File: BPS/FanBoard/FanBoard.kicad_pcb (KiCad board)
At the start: 2 copper layers, 31.8 x 38.1 mm, 18 parts, among them J1 Conn_01x02, J2 Conn_01x02, J3 Conn_01x02, J4 Conn_01x02, Q1 BUK9M34-100EX, Q2 BUK9M34-100EX, Q3 BUK9M34-100EX, Q4 BUK9M34-100EX

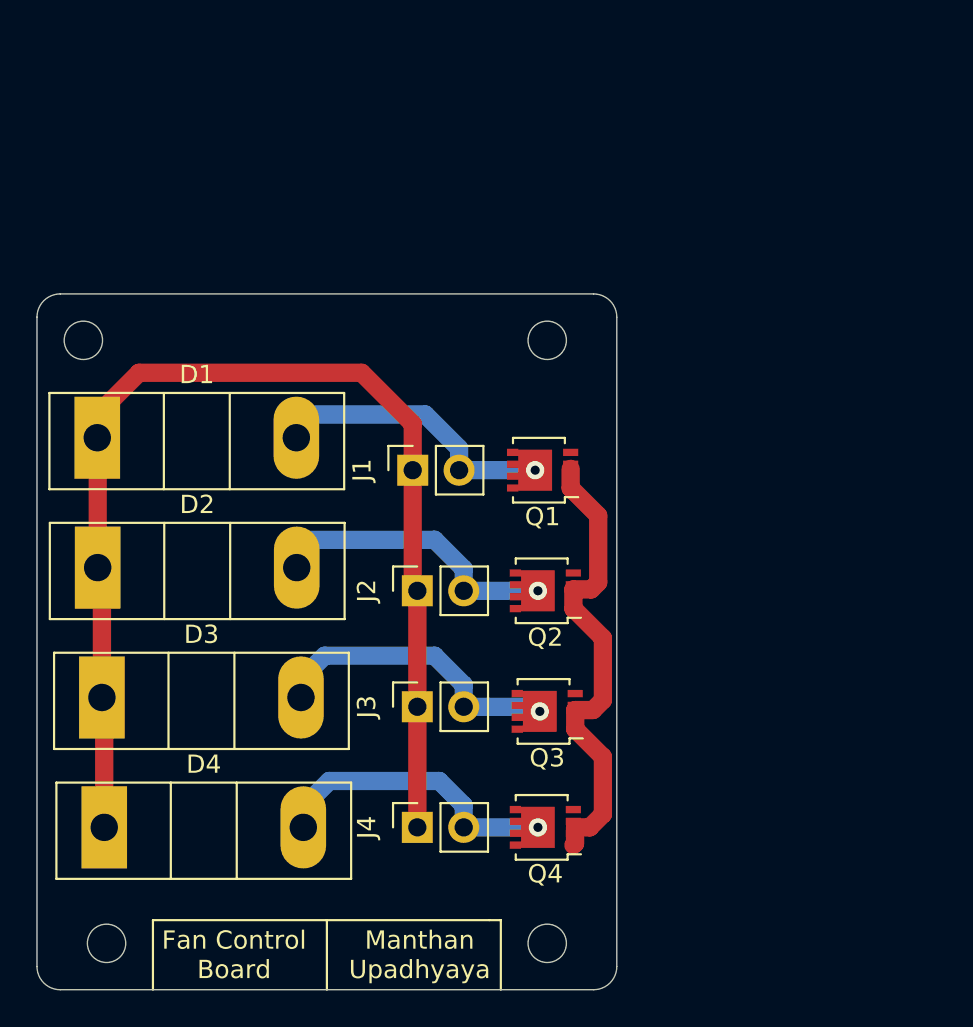
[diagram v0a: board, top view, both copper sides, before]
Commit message: Finished Fan Board PCB
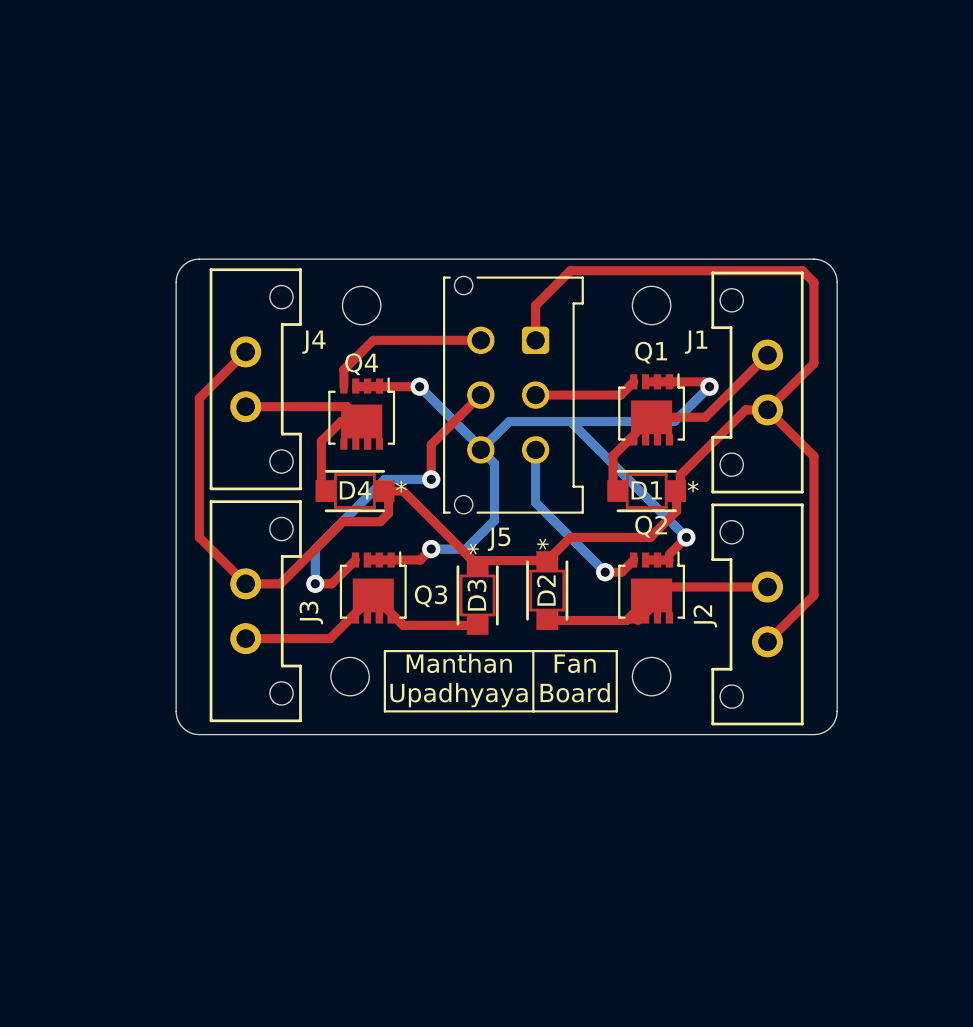
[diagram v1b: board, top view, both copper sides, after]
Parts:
- removed the G*** at (146.7, 89.5)
- removed the REF** at (134.6, 69.8)
- removed the REF** at (135.9, 102.9)
- removed the REF** at (160.0, 102.9)
- removed the REF** at (160.0, 69.8)
- added G***: LOGO, UTSVT_Special:Hallock_Image_Small, B.Cu at (165.4, 77.7)
- added J5: LDRBRDConn, Connector_Molex:Molex_Micro-Fit_3.0_43045-0612_2x03_P3.00mm_Vertical, F.Cu at (159.4, 69.8)
- added REF**: MountingHole_2.1mm, MountingHole:MountingHole_2.1mm, F.Cu at (165.7, 67.9)
- added REF**: MountingHole_2.1mm, MountingHole:MountingHole_2.1mm, F.Cu at (149.9, 67.9)
- added REF**: MountingHole_2.1mm, MountingHole:MountingHole_2.1mm, F.Cu at (165.7, 88.3)
- added REF**: MountingHole_2.1mm, MountingHole:MountingHole_2.1mm, F.Cu at (149.2, 88.3)
- D1, D2, D3, D4: value C3D25170H -> V22F22HM3; footprint Package_TO_SOT_THT:TO-247-2_Vertical -> UTSVT_BPS:V2F22HM
- J1, J2, J3, J4: footprint Connector_PinSocket_2.54mm:PinSocket_1x02_P2.54mm_Vertical -> UTSVT_Connectors:Molex_MicroFit3.0_1x2xP3.00mm_PolarizingPeg_Vertical
- moved D1 30.2 mm to (165.5, 78.1), turned to 180 degrees
- moved J4 27.7 mm to (143.5, 70.5), turned to 270 degrees
- moved Q4 24.8 mm to (149.9, 73.9), turned to 270 degrees
- moved D2 24.6 mm to (160.0, 83.6), turned to 270 degrees
- moved D4 23.0 mm to (149.5, 78.1), turned to 180 degrees
- moved D3 21.3 mm to (156.2, 83.8), turned to 270 degrees
- moved G*** 20.5 mm to (149.6, 75.2), turned to 180 degrees
- moved J1 19.7 mm to (172.1, 73.7)
- moved J2 19.4 mm to (172.1, 86.4)
- moved Q3 11.7 mm to (150.5, 83.4), turned to 270 degrees
- moved J3 11.6 mm to (143.5, 83.2), turned to 270 degrees
- moved Q1 6.82 mm to (165.7, 73.7), turned to 270 degrees
- moved Q2 5.82 mm to (165.7, 83.4), turned to 270 degrees
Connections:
- net GND renamed GNDPWR
- Q1 pad 4: Net-(Q1-Pad4) -> /FAN1
- Q2 pad 4: Net-(Q2-Pad4) -> /FAN2
- Q3 pad 4: Net-(Q3-Pad4) -> /FAN3
- Q4 pad 4: Net-(Q4-Pad4) -> /FAN4
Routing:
- net +12V: track 64.3 -> 93.6 mm
- net GNDPWR: track 26.0 -> 49.4 mm, vias 0 -> 4
- net /FAN3: track 0.00 -> 18.3 mm, vias 0 -> 2
- net /FAN2: track 0.00 -> 10.2 mm, vias 0 -> 1
- net /FAN4: track 0.00 -> 9.06 mm
- net /FAN1: track 0.00 -> 5.68 mm
- net Net-(D4-Pad2): track 16.3 -> 12.1 mm, vias 1 -> 0
- net Net-(D1-Pad2): track 15.9 -> 12.7 mm, vias 1 -> 0
- net Net-(D2-Pad2): track 16.3 -> 13.9 mm, vias 1 -> 0
- net Net-(D3-Pad2): track 16.6 -> 14.4 mm, vias 1 -> 0
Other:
- board size 31.8 x 38.1 mm -> 36.2 x 26 mm
- board text added: "Fan Board"
- board text removed: "Fan Control Board"

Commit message: Redid layout of board
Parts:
- removed G***: LOGO, UTSVT_Special:Hallock_Image_Small
- removed G***: LOGO, UTSVT_Special:UTSVT_Logo_Symbol
- removed J1: Conn_01x02, UTSVT_Connectors:Molex_MicroFit3.0_1x2xP3.00mm_PolarizingPeg_Vertical
- removed J5: LDRBRDConn, Connector_Molex:Molex_Micro-Fit_3.0_43045-0612_2x03_P3.00mm_Vertical
- removed REF** (x4): MountingHole_2.1mm, MountingHole:MountingHole_2.1mm
- added FAN1: Conn_01x02, UTSVT_Connectors:Molex_MicroFit3.0_1x2xP3.00mm_PolarizingPeg_Vertical, F.Cu at (176.3, 80.8)
- added H1: MountingHole, MountingHole:MountingHole_3mm, F.Cu at (146.1, 59.7)
- added H2: MountingHole, MountingHole:MountingHole_3mm, F.Cu at (146.1, 85.1)
- added H3: MountingHole, MountingHole:MountingHole_3mm, F.Cu at (168.9, 59.7)
- added H4: MountingHole, MountingHole:MountingHole_3mm, F.Cu at (168.9, 85.1)
- added LDRBRDConn: LDRBRDConn, Connector_Molex:Molex_Micro-Fit_3.0_43045-0612_2x03_P3.00mm_Vertical, F.Cu at (161.0, 66.4)
- moved FAN3 36.4 mm to (176.2, 67.3), turned to 90 degrees
- moved FAN2 33.9 mm to (139.1, 78.2), turned to 270 degrees
- moved Q3 25.2 mm to (168.1, 65.5), turned to 0 degrees
- moved D3 24.1 mm to (172.0, 65.7), turned to 90 degrees
- moved Q2 18.9 mm to (147.3, 79.6), turned to 180 degrees
- moved D2 17.0 mm to (143.4, 79.6)
- moved D4 13.6 mm to (143.7, 65.8), turned to 270 degrees
- moved Q4 8.02 mm to (148.0, 66.1), turned to 180 degrees
- moved FAN4 7.61 mm to (139.1, 64.3)
- moved D1 6.55 mm to (171.9, 79.4), turned to 90 degrees
- moved Q1 5.60 mm to (167.6, 78.9), turned to 0 degrees
- renumbered J2 to FAN2, J3 to FAN3, J4 to FAN4
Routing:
- net +12V: track 93.6 -> 0.00 mm, vias 0 -> 4
- net GNDPWR: track 49.4 -> 0.00 mm, vias 4 -> 0
- net /FAN1: track 5.68 -> 19.6 mm, vias 0 -> 1
- net Net-(D3-Pad2): track 14.4 -> 8.37 mm
- net Net-(D2-Pad2): track 13.9 -> 8.39 mm
- net /FAN2: track 10.2 -> 15.0 mm
- net Net-(D1-Pad2): track 12.7 -> 8.84 mm
- net Net-(D4-Pad2): track 12.1 -> 9.08 mm
- net /FAN4: track 9.06 -> 7.58 mm, vias 0 -> 1
- net /FAN3: track 18.3 -> 17.8 mm, vias 2 -> 1
- added copper zone on B.Cu, net +12V
- added copper zone on F.Cu, net GNDPWR
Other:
- board outline removed
- board text added: "12V"
- board text added: "FAN1"
- board text added: "FAN2"
- board text added: "FAN3"
- board text added: "FAN4"
- board text added: "GND"

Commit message: Finishing touches
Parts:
- added G***: LOGO, UTSVT_Special:Hallock_Image_Small, B.Cu at (152.4, 75.6)
- added G***: LOGO, UTSVT_Special:UTSVT_Logo_Symbol, B.Cu at (166.4, 76.2)
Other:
- board outline added: 45.1 x 33 mm

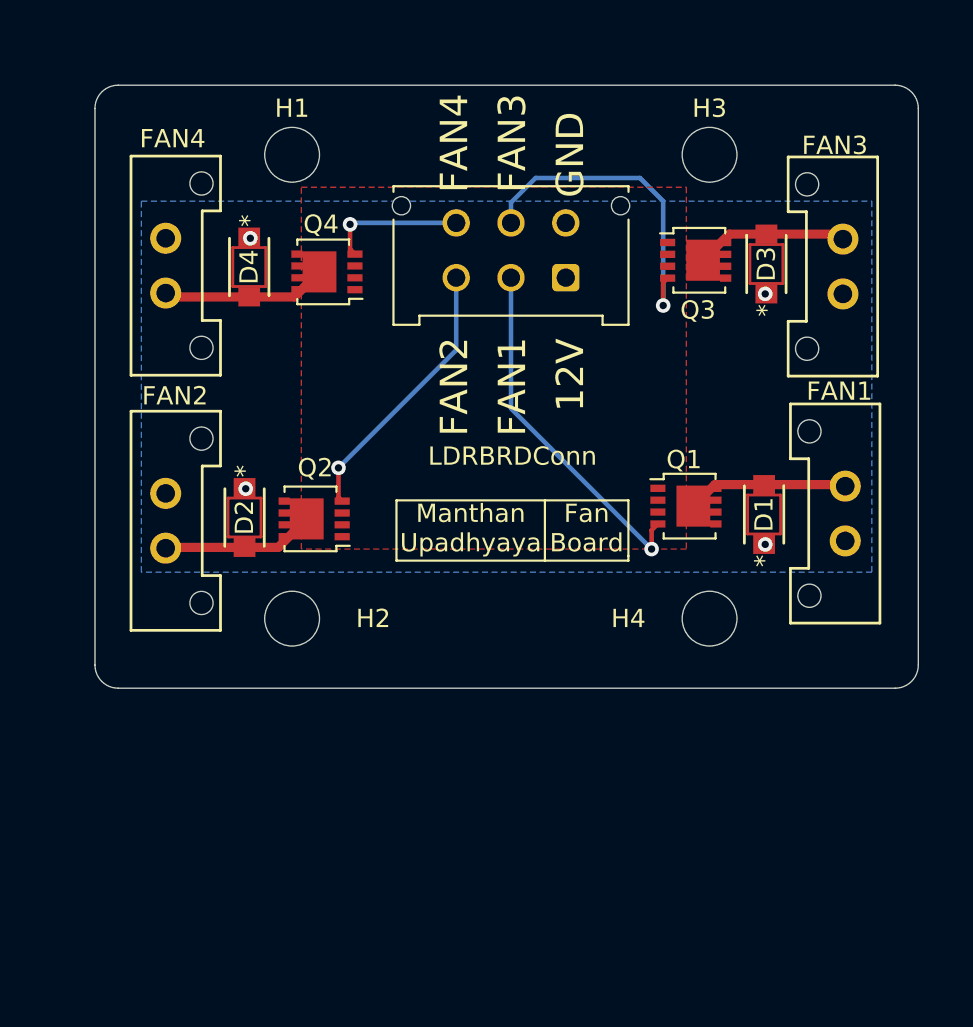
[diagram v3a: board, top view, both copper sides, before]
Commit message: Added status LED
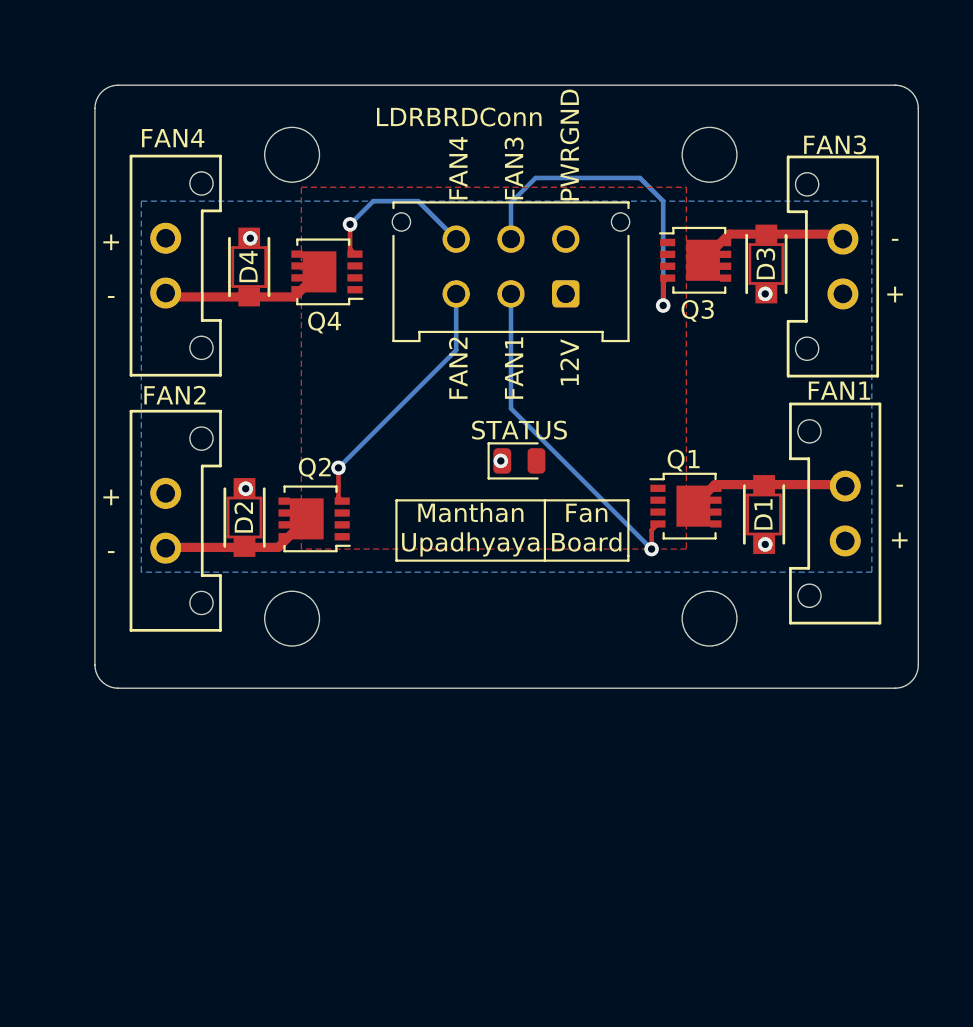
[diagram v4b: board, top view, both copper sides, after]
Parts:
- added STATUS: LED, LED_SMD:LED_0805_2012Metric, F.Cu at (158.5, 76.5)
- LDRBRDConn: value LDRBRDConn -> Conn_02x03
- moved LDRBRDConn 0.89 mm to (161.0, 67.3)
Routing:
- net /FAN4: track 7.58 -> 9.05 mm
- net /FAN3: track 17.8 -> 18.7 mm
- net /FAN2: track 15.0 -> 14.1 mm
- net /FAN1: track 19.6 -> 18.7 mm
- net +12V: vias 4 -> 5
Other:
- board text added: "+"
- board text added: "-"
- board text added: "PWRGND"
- board text removed: "GND"

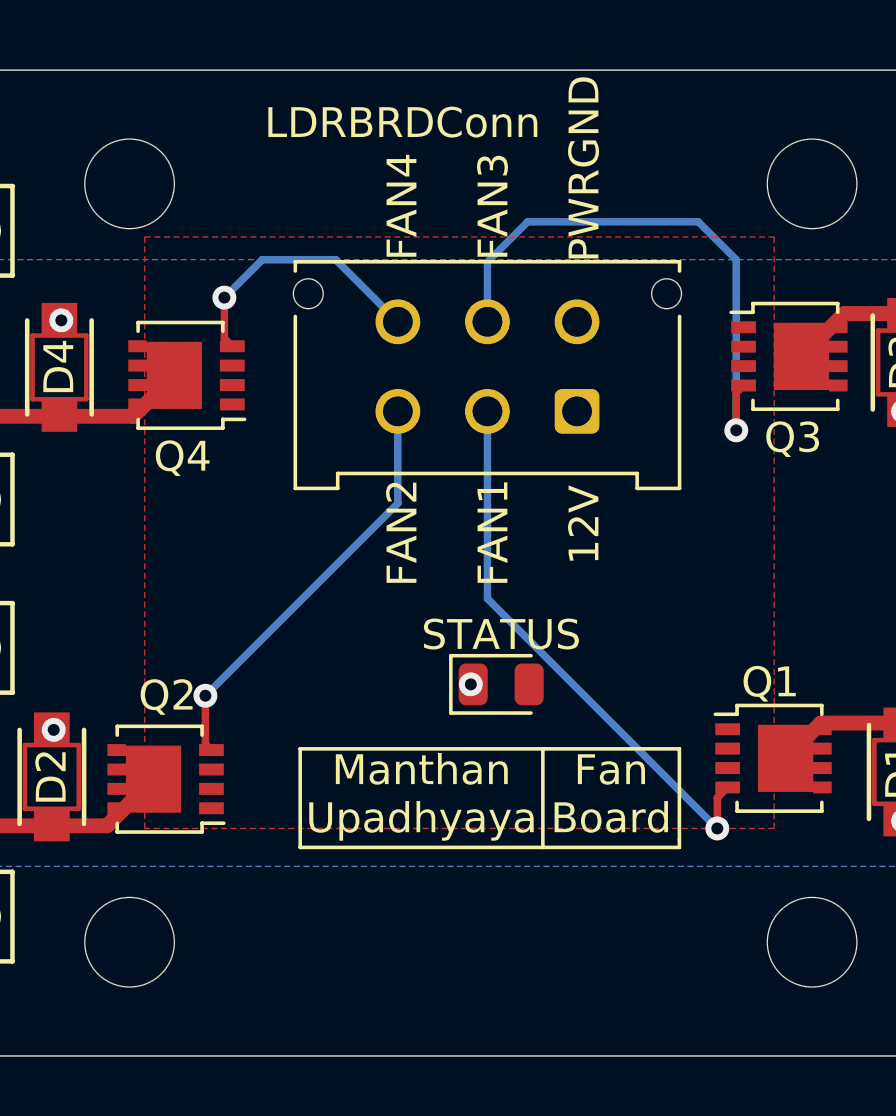
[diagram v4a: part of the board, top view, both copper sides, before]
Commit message: Added silkscreen comments
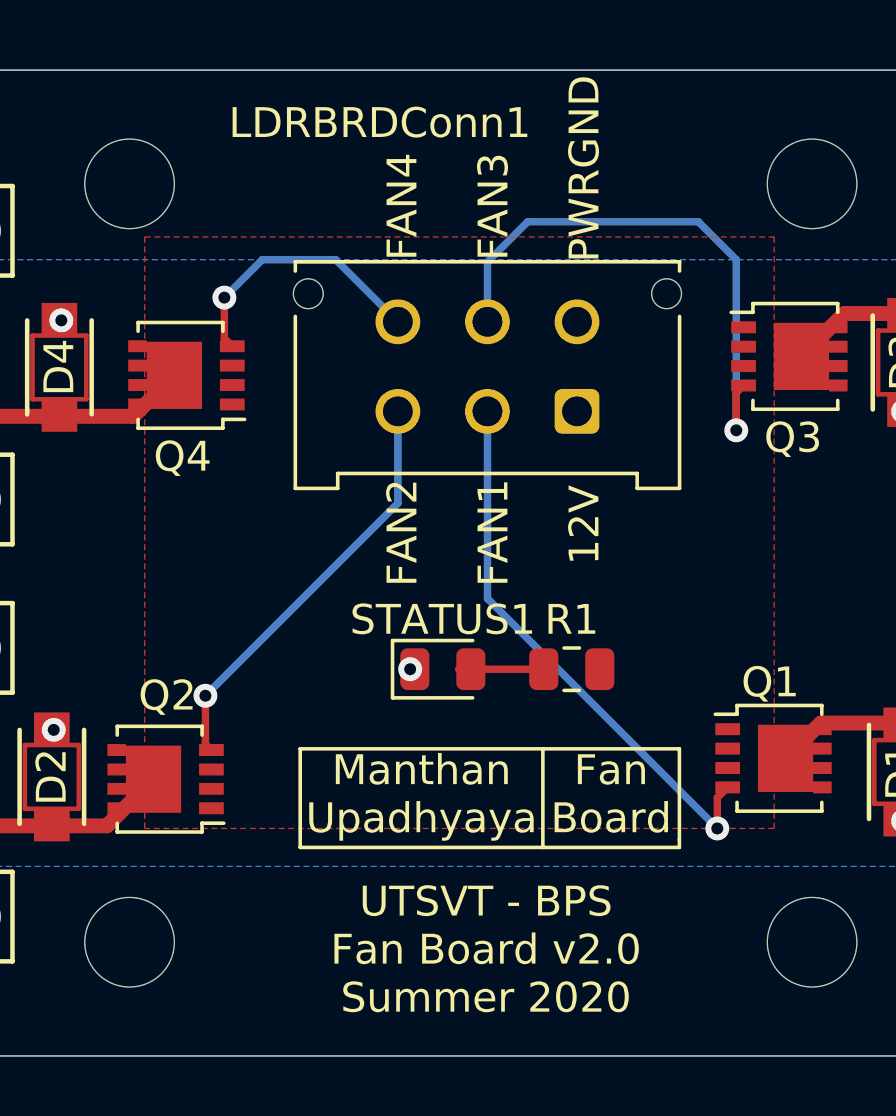
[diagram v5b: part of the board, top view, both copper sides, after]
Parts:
- added R1: 45k, Resistor_SMD:R_0805_2012Metric, F.Cu at (160.9, 75.9)
- moved STATUS1 2.02 mm to (156.5, 75.9)
- renumbered LDRBRDConn to LDRBRDConn1, STATUS to STATUS1
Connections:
- STATUS1 pad 2: GNDPWR -> Net-(R1-Pad1)
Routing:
- net Net-(R1-Pad1): track 0.00 -> 2.95 mm
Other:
- board text added: "UTSVT - BPS Fan Board v2.0 Summer 2020"
